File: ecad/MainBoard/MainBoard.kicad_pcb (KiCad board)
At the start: 2 copper layers, 34.6 x 88.7 mm, 10 parts, among them J1 ACJM-HHDR, J2 PJ-102A, J3 toEffectsBoard, J4 ACJM-HHDR, U1 FS57003PLT2B2M2QE

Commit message: Big commit
Spice Simulations
Finalize ECAD schematic
old MCAD stuff
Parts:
- added C10: CP, Capacitor_SMD:C_0805_2012Metric_Pad1.18x1.45mm_HandSolder, B.Cu at (88.8, 100.3)
- added C11: 20n, Capacitor_SMD:C_0805_2012Metric_Pad1.18x1.45mm_HandSolder, B.Cu at (107.9, 132.3)
- added C4: 1u, Capacitor_SMD:C_0805_2012Metric_Pad1.18x1.45mm_HandSolder, B.Cu at (113.2, 126.7)
- added C5: 51p, Capacitor_SMD:C_0805_2012Metric_Pad1.18x1.45mm_HandSolder, B.Cu at (110.2, 96.7)
- added C6: 0u22, Capacitor_SMD:C_0805_2012Metric_Pad1.18x1.45mm_HandSolder, B.Cu at (102.2, 100.6)
- added C7: 220n, Capacitor_SMD:C_0805_2012Metric_Pad1.18x1.45mm_HandSolder, B.Cu at (101.0, 76.8)
- added C8: 1u, Capacitor_SMD:C_0805_2012Metric_Pad1.18x1.45mm_HandSolder, B.Cu at (93.3, 90.3)
- added C9: 0u1, Capacitor_SMD:C_0805_2012Metric_Pad1.18x1.45mm_HandSolder, B.Cu at (86.2, 90.6)
- added D2: QBL8XX60D, digikey-footprints:LED_5mm_Radial, F.Cu at (101.3, 105.8)
- added D3: 1N914, Diode_THT:D_DO-35_SOD27_P2.54mm_Vertical_AnodeUp, F.Cu at (111.7, 80.1)
- added D4: 1N914, Diode_THT:D_DO-35_SOD27_P2.54mm_Vertical_AnodeUp, F.Cu at (114.3, 77.6)
- added G***: LOGO, screaming-panda:Panda_Logo, F.Cu at (113.7, 72.4)
- added J5: TonePot, Connector_PinHeader_2.54mm:PinHeader_1x03_P2.54mm_Vertical, F.Cu at (102.5, 79.8)
- added J6: VolumePot, Connector_PinHeader_2.54mm:PinHeader_1x03_P2.54mm_Vertical, F.Cu at (93.3, 83.3)
- added Q1: 2N4401BU, digikey-footprints:TO-92-3, F.Cu at (88.8, 92.9)
- added Q2: 2N4401BU, digikey-footprints:TO-92-3, F.Cu at (109.7, 125.0)
- added R10: 1k, Resistor_SMD:R_0805_2012Metric_Pad1.20x1.40mm_HandSolder, B.Cu at (93.3, 86.6)
- added R11: 501k, Resistor_SMD:R_0805_2012Metric_Pad1.20x1.40mm_HandSolder, B.Cu at (84.2, 90.6)
- added R12: 10k, Resistor_SMD:R_0805_2012Metric_Pad1.20x1.40mm_HandSolder, B.Cu at (85.9, 95.5)
- added R13: 100, Resistor_SMD:R_0805_2012Metric_Pad1.20x1.40mm_HandSolder, B.Cu at (88.8, 96.5)
- added R14: 10k, Resistor_SMD:R_0805_2012Metric_Pad1.20x1.40mm_HandSolder, B.Cu at (86.8, 100.3)
- added R15: 1M5, Resistor_SMD:R_0805_2012Metric_Pad1.20x1.40mm_HandSolder, B.Cu at (108.8, 135.2)
- added R16: 1k, Resistor_SMD:R_0805_2012Metric_Pad1.20x1.40mm_HandSolder, B.Cu at (107.9, 128.5)
- added R17: 501k, Resistor_SMD:R_0805_2012Metric_Pad1.20x1.40mm_HandSolder, B.Cu at (106.0, 126.5)
- added R18: 10k, Resistor_SMD:R_0805_2012Metric_Pad1.20x1.40mm_HandSolder, B.Cu at (111.2, 128.8)
- added R2: 10k, Resistor_SMD:R_0805_2012Metric_Pad1.20x1.40mm_HandSolder, B.Cu at (89.8, 70.5)
- added R3: 10k, Resistor_SMD:R_0805_2012Metric_Pad1.20x1.40mm_HandSolder, B.Cu at (91.8, 74.2)
- added R4: 10k, Resistor_SMD:R_0805_2012Metric_Pad1.20x1.40mm_HandSolder, B.Cu at (114.2, 123.8)
- added R5: 51k, Resistor_SMD:R_0805_2012Metric_Pad1.20x1.40mm_HandSolder, B.Cu at (115.0, 84.6)
- added R6: 1k, Resistor_SMD:R_0805_2012Metric_Pad1.20x1.40mm_HandSolder, B.Cu at (104.4, 97.7)
- added R7: 10k, Resistor_SMD:R_0805_2012Metric_Pad1.20x1.40mm_HandSolder, B.Cu at (104.2, 100.6)
- added R8: 220, Resistor_SMD:R_0805_2012Metric_Pad1.20x1.40mm_HandSolder, B.Cu at (101.0, 74.9)
- added R9: 1k, Resistor_SMD:R_0805_2012Metric_Pad1.20x1.40mm_HandSolder, B.Cu at (99.4, 94.2)
- added U2: RC4558, Package_SO:Texas_R-PDSO-G8_EP2.95x4.9mm_Mask2.4x3.1mm, B.Cu at (104.5, 93.9)
- C1, R1: moved to B.Cu
- C2: value 1u -> 10n; moved to B.Cu
- C3: value 10n -> 47u; moved to B.Cu
- D1: value QBL8XX60D -> 1N914; footprint Diode_THT:D_DO-201AD_P3.81mm_Vertical_AnodeUp -> Diode_THT:D_DO-35_SOD27_P2.54mm_Vertical_AnodeUp
- J3: value toEffectsBoard -> ACJM-HHDR; footprint Connector_PinHeader_1.27mm:PinHeader_2x02_P1.27mm_Vertical -> screaming-panda:ACJM-HHDR
- J4: value ACJM-HHDR -> DrivePot; footprint screaming-panda:ACJM-HHDR -> Connector_PinHeader_2.54mm:PinHeader_1x03_P2.54mm_Vertical
- moved D1 39.2 mm to (91.1, 67.3)
- moved J3 15.6 mm to (105.8, 93.8)
- moved J4 11.7 mm to (111.7, 83.6), turned to 270 degrees
- moved C1 8.35 mm to (93.7, 70.5), turned to 270 degrees
- moved C3 8.34 mm to (89.8, 74.2), turned to 270 degrees
- moved C2 6.24 mm to (91.8, 70.5), turned to 270 degrees
- moved R1 1.82 mm to (104.5, 106.8), turned to 90 degrees
- moved J1 0.22 mm to (94.2, 117.8)
- moved U1 0.10 mm to (100.0, 135.6), turned to 180 degrees
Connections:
- C3 pad 1: +9V -> VCC
- D1 pad 1: Net-(D1-Pad1) -> +9V
- D1 pad 2: Net-(D1-Pad2) -> GND
- R1 pad 2: Net-(D1-Pad2) -> Net-(D2-Pad2)
- U1 pad 1: Net-(D1-Pad1) -> Net-(D2-Pad1)
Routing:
- net /SIG_OUT: track 0.00 -> 50.7 mm
- net Net-(D1-Pad1): track 37.8 -> 0.00 mm
- net /tone/IN: track 0.00 -> 35.9 mm, vias 0 -> 1
- net /EFFECT_OUT: track 0.00 -> 35.1 mm, vias 0 -> 1
- net Net-(C4-Pad2): track 0.00 -> 34.2 mm, vias 0 -> 2
- net Net-(C5-Pad1): track 0.00 -> 33.1 mm, vias 0 -> 2
- net Net-(C5-Pad2): track 0.00 -> 28.9 mm, vias 0 -> 2
- net Net-(D2-Pad1): track 0.00 -> 27.8 mm
- net Net-(J5-Pad3): track 0.00 -> 24.1 mm, vias 0 -> 1
- net /PassThru: track 0.00 -> 20.1 mm
- net VCC: track 0.00 -> 19.9 mm, vias 0 -> 3
- net +9V: track 0.00 -> 13.8 mm, vias 0 -> 1
- net GND: track 12.0 -> 0.00 mm
- net /SIG_IN: track 0.00 -> 10.7 mm
- net /volume/IN: track 0.00 -> 10.5 mm, vias 0 -> 2
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- added copper zone on In1.Cu, net +9V
- added copper zone on F.Cu, net GND
- added copper zone on In2.Cu, net VCC
- removed copper zone on F.Cu, net +9V
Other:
- copper layers 2 -> 4

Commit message: Update BOM and SPIRCE SIM
Add netlist to calculate power dissipation through each resistor
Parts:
- added C3: 50p, Capacitor_SMD:C_0805_2012Metric_Pad1.18x1.45mm_HandSolder, F.Cu at (94.9, 30.7)
- added IC1: RC4558, Package_SO:Texas_R-PDSO-G8_EP2.95x4.9mm_Mask2.4x3.1mm, F.Cu at (81.8, 32.4)
- added R6: 4k7, Resistor_SMD:R_0805_2012Metric_Pad1.20x1.40mm_HandSolder, F.Cu at (99.7, 30.7)
- C11: renamed from C10; value CP -> 10u
- C4: renamed from C5; value 51p -> 50p
- renumbered C11 to C1, C9 to C10, C1 to C12, C4 to C2, C6 to C5, C3 to C7, C7 to C9, D3 to D1, D4 to D2, D2 to D4, D1 to D5, J3 to J2, J2 to J3, Q2 to Q1, Q1 to Q2, R16 to R1, R3 to R10, R8 to R11, R11 to R12, R14 to R13, R12 to R14, R13 to R15, R7 to R16, R9 to R17, R10 to R18, J4 to R19, R17 to R2, J5 to R20, J6 to R21, R15 to R22, R1 to R23, R18 to R3, R4 to R5, R5 to R7, R6 to R8, R2 to R9, U1 to SW1
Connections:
- C10 pad 2: Net-(C9-Pad2) (its old number) -> Net-(C10-Pad2)
- C12 pad 2: GND -> 0
- C2 pad 2: Net-(C4-Pad2) -> Net-(C2-Pad2)
- C4 pad 1: Net-(C5-Pad1) -> Net-(C3-Pad1)
- C4 pad 2: Net-(C5-Pad2) -> Net-(C4-Pad2)
- C5 pad 2: GND -> 0
- C7 pad 2: GND -> 0
- D1 pad 1: Net-(C5-Pad1) -> Net-(C3-Pad1)
- D1 pad 2: Net-(C5-Pad2) -> Net-(C4-Pad2)
- D2 pad 1: Net-(C5-Pad2) -> Net-(C4-Pad2)
- D2 pad 2: Net-(C5-Pad1) -> Net-(C3-Pad1)
- D4 pad 1: Net-(D2-Pad1) -> Net-(D4-Pad1)
- D5 pad 2: GND -> 0
- J1 pad S: GND -> 0
- J1 pad SN: GND -> 0
- J1 pad TN: GND -> 0
- J2 pad S: GND -> 0
- J2 pad SN: (no net) -> Net-(J2-PadSN)
- J2 pad TN: (no net) -> Net-(J2-PadTN)
- J3 pad 1: GND -> 0
- J3 pad 3: GND -> 0
- R10 pad 2: GND -> 0
- R11 pad 2: GND -> 0
- R12 pad 2: GND -> VCC
- R13 pad 2: GND -> 0
- R14 pad 2: GND -> 0
- R17 pad 2: Net-(J5-Pad3) -> Net-(IC1-Pad6)
- R19 pad 1: Net-(J4-Pad1) -> Net-(R19-Pad1)
- R19 pad 2: (no net) -> Net-(C4-Pad2)
- R19 pad 3: Net-(C5-Pad1) -> Net-(R19-Pad3)
- R20 pad 3: Net-(J5-Pad3) -> Net-(IC1-Pad6)
- R21 pad 2: VCC -> Net-(C10-Pad2)
- R21 pad 3: Net-(C9-Pad2) (its old number) -> VCC
- R22 pad 2: GND -> 0
- R3 pad 2: GND -> 0
- R5 pad 2: Net-(C4-Pad2) -> Net-(C2-Pad2)
- R7 pad 1: Net-(J4-Pad1) -> Net-(R19-Pad3)
- R7 pad 2: Net-(C5-Pad2) -> Net-(C3-Pad1)
- R8 pad 2: Net-(C5-Pad1) -> Net-(C4-Pad2)
- SW1 pad 1: Net-(D2-Pad1) -> /PassThru
- SW1 pad 2: GND -> /SIG_IN
- SW1 pad 4: /PassThru -> Net-(D4-Pad1)
- SW1 pad 5: /SIG_IN -> 0
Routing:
- net Net-(C9-Pad2): track 1.99 -> 9.06 mm
- net Net-(C9-Pad2) (its old number): track 7.07 -> 0.00 mm
- added copper zone on F.Cu, net /SIG_IN
- added copper zone on B.Cu, net VCC
- removed copper zone on B.Cu, net GND
- removed copper zone on F.Cu, net GND

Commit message: Clean up ecad
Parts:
- removed the C2 at (113.2, 126.7)
- removed the C2 at (91.8, 70.5)
- removed Q1, Q2: 2N4401BU, digikey-footprints:TO-92-3
- removed U2: RC4558, Package_SO:Texas_R-PDSO-G8_EP2.95x4.9mm_Mask2.4x3.1mm
- added C2: 1u, Capacitor_SMD:C_0603_1608Metric_Pad1.08x0.95mm_HandSolder, F.Cu at (52.7, 66.2)
- C1, C5: footprint Capacitor_SMD:C_0805_2012Metric_Pad1.18x1.45mm_HandSolder -> Capacitor_SMD:C_0402_1005Metric_Pad0.74x0.62mm_HandSolder; moved to F.Cu
- C10, C4: footprint Capacitor_SMD:C_0805_2012Metric_Pad1.18x1.45mm_HandSolder -> Capacitor_SMD:C_0201_0603Metric_Pad0.64x0.40mm_HandSolder; moved to F.Cu
- C11, C8: footprint Capacitor_SMD:C_0805_2012Metric_Pad1.18x1.45mm_HandSolder -> Capacitor_SMD:C_0603_1608Metric_Pad1.08x0.95mm_HandSolder; moved to F.Cu
- C12: footprint Capacitor_SMD:C_0805_2012Metric_Pad1.18x1.45mm_HandSolder -> Capacitor_SMD:C_1210_3225Metric_Pad1.33x2.70mm_HandSolder; moved to F.Cu
- C3: footprint Capacitor_SMD:C_0805_2012Metric_Pad1.18x1.45mm_HandSolder -> Capacitor_SMD:C_0201_0603Metric_Pad0.64x0.40mm_HandSolder
- C7, C9: footprint Capacitor_SMD:C_0805_2012Metric_Pad1.18x1.45mm_HandSolder -> Capacitor_SMD:C_1206_3216Metric_Pad1.33x1.80mm_HandSolder; moved to F.Cu
- G***: moved to B.Cu
- IC1: footprint Package_SO:Texas_R-PDSO-G8_EP2.95x4.9mm_Mask2.4x3.1mm -> DigiKey:SOIC-8_W3.9mm
- R1, R17, R18, R22, R23, R8: footprint Resistor_SMD:R_0805_2012Metric_Pad1.20x1.40mm_HandSolder -> Resistor_SMD:R_0402_1005Metric_Pad0.72x0.64mm_HandSolder; moved to F.Cu
- R10, R13, R14, R16, R3, R5, R9: moved to F.Cu
- R11: footprint Resistor_SMD:R_0805_2012Metric_Pad1.20x1.40mm_HandSolder -> Resistor_SMD:R_2512_6332Metric_Pad1.40x3.35mm_HandSolder; moved to F.Cu
- R12: value 501k -> 510k; moved to F.Cu
- R15: footprint Resistor_SMD:R_0805_2012Metric_Pad1.20x1.40mm_HandSolder -> Resistor_SMD:R_1218_3246Metric_Pad1.22x4.75mm_HandSolder; moved to F.Cu
- R19: value DrivePot -> 500ka
- R2: value 501k -> 505k; moved to F.Cu
- R20: value TonePot -> 20kb
- R21: value VolumePot -> 20ka
- R7: footprint Resistor_SMD:R_0805_2012Metric_Pad1.20x1.40mm_HandSolder -> Resistor_SMD:R_1206_3216Metric_Pad1.30x1.75mm_HandSolder; moved to F.Cu
- moved R5 87.5 mm to (48.2, 66.4), turned to 0 degrees
- moved R23 84.9 mm to (40.9, 50.4), turned to 0 degrees
- moved R22 83.1 mm to (64.5, 64.8)
- moved R3 78.2 mm to (70.0, 62.3), turned to 0 degrees
- moved C1 77.0 mm to (71.0, 64.8), turned to 0 degrees
- moved R2 76.0 mm to (65.3, 62.3), turned to 0 degrees
- moved R1 75.3 mm to (67.8, 64.8), turned to 0 degrees
- moved R7 69.5 mm to (48.8, 63.3), turned to 0 degrees
- moved R18 66.8 mm to (28.9, 68.9), turned to 0 degrees
- moved R15 66.6 mm to (30.2, 64.8), turned to 0 degrees
- moved R16 62.6 mm to (54.1, 63.1), turned to 0 degrees
- moved C4 62.3 mm to (56.3, 65.5), turned to 0 degrees
- moved C11 62.1 mm to (35.3, 68.8), turned to 0 degrees
- moved R13 61.7 mm to (35.5, 66.0), turned to 0 degrees
- moved R17 60.8 mm to (57.3, 50.4), turned to 0 degrees
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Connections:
- C8 pad 1: Net-(C8-Pad1) -> /volume/IN
- C8 pad 2: /volume/IN -> Net-(C8-Pad2)
- J2 pad SN: Net-(J2-PadSN) -> 0
- J2 pad TN: Net-(J2-PadTN) -> 0
- R11 pad 1: Net-(C9-Pad2) -> Net-(C9-Pad1)
- R12 pad 1: Net-(C10-Pad1) -> VCC
- R12 pad 2: VCC -> Net-(C10-Pad1)
- R18 pad 2: Net-(C8-Pad1) -> Net-(C8-Pad2)
- R20 pad 2: Net-(C9-Pad1) -> Net-(C9-Pad2)
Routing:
- net /SIG_OUT: track 50.7 -> 0.00 mm
- net /tone/IN: track 35.9 -> 0.00 mm, vias 1 -> 0
- net /EFFECT_OUT: track 35.1 -> 0.00 mm, vias 1 -> 0
- net Net-(C4-Pad2): track 34.2 -> 0.00 mm, vias 2 -> 0
- net Net-(C5-Pad1): track 33.1 -> 0.00 mm, vias 2 -> 0
- net Net-(C5-Pad2): track 28.9 -> 0.00 mm, vias 2 -> 0
- net Net-(D2-Pad1): track 27.8 -> 0.00 mm
- net Net-(J5-Pad3): track 24.1 -> 0.00 mm, vias 1 -> 0
- net 0: track 0.00 -> 21.2 mm
- net /PassThru: track 20.1 -> 0.00 mm
- net VCC: track 19.9 -> 0.00 mm, vias 3 -> 0
- net /SIG_IN: track 10.7 -> 0.00 mm
- net /volume/IN: track 10.5 -> 0.00 mm, vias 2 -> 0
- net Net-(C9-Pad2): track 9.06 -> 0.00 mm
- net Net-(Q1-Pad2): track 7.05 -> 0.00 mm
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- added copper zone on B.Cu, net 0
- added copper zone on F.Cu, net VCC
- removed copper zone on In1.Cu, net +9V
- removed copper zone on F.Cu, net /SIG_IN
- removed copper zone on B.Cu, net VCC
- removed copper zone on In2.Cu, net VCC
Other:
- copper layers 4 -> 2

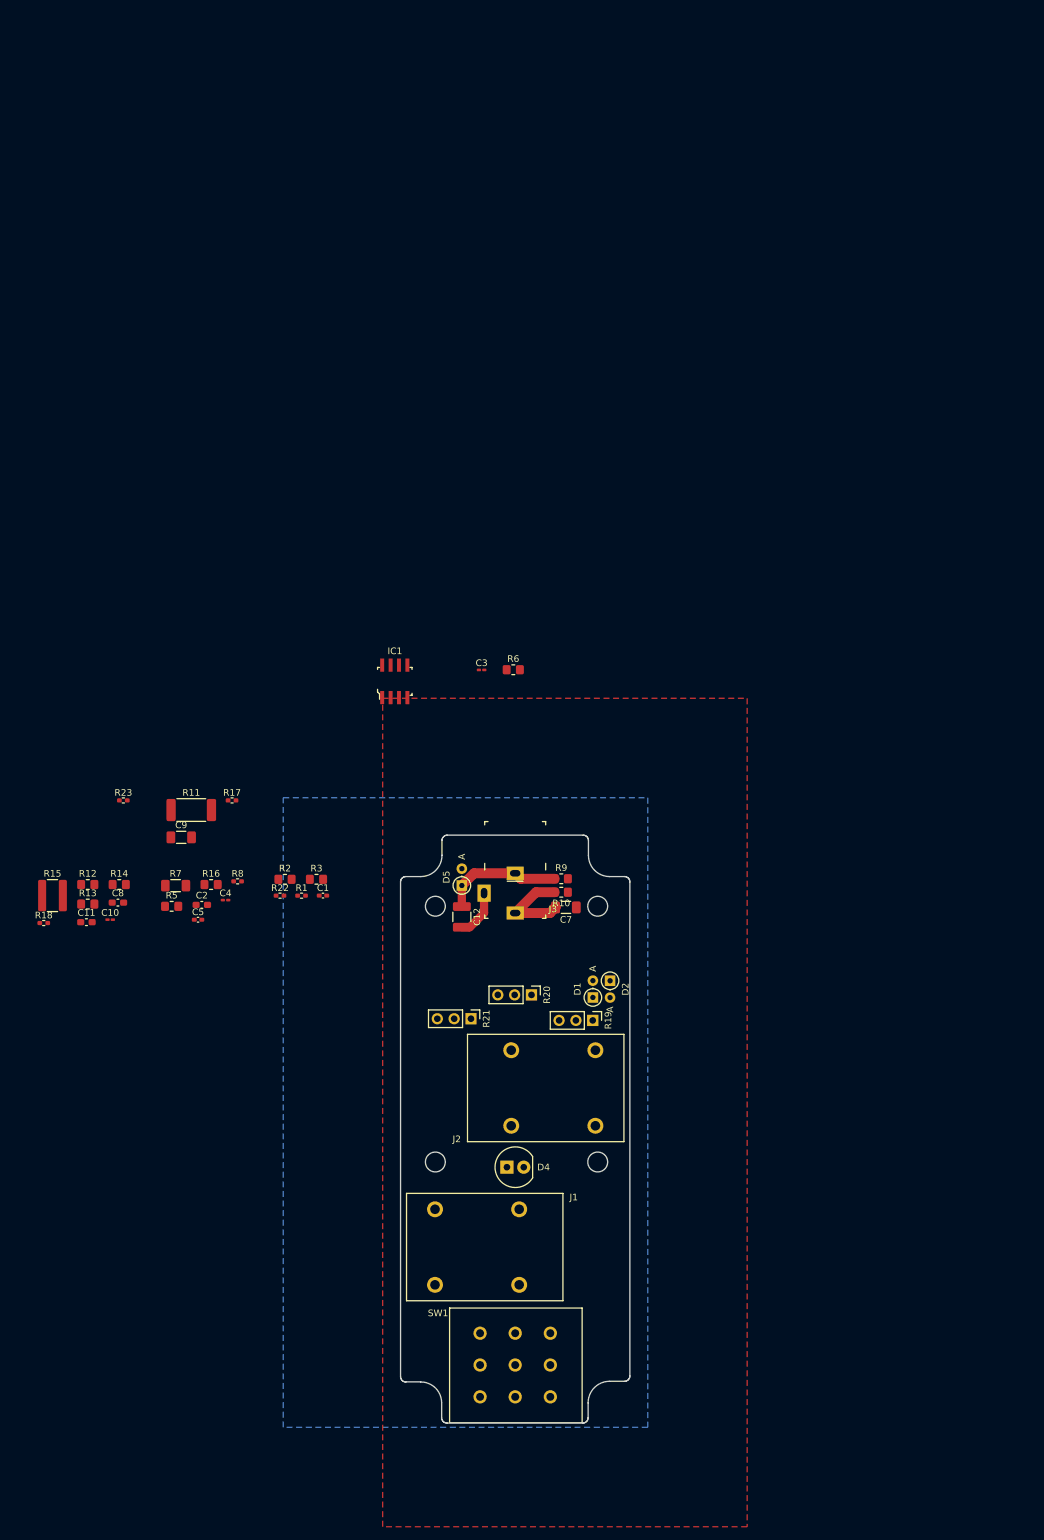
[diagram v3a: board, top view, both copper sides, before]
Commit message: Update layouts with finished mcad
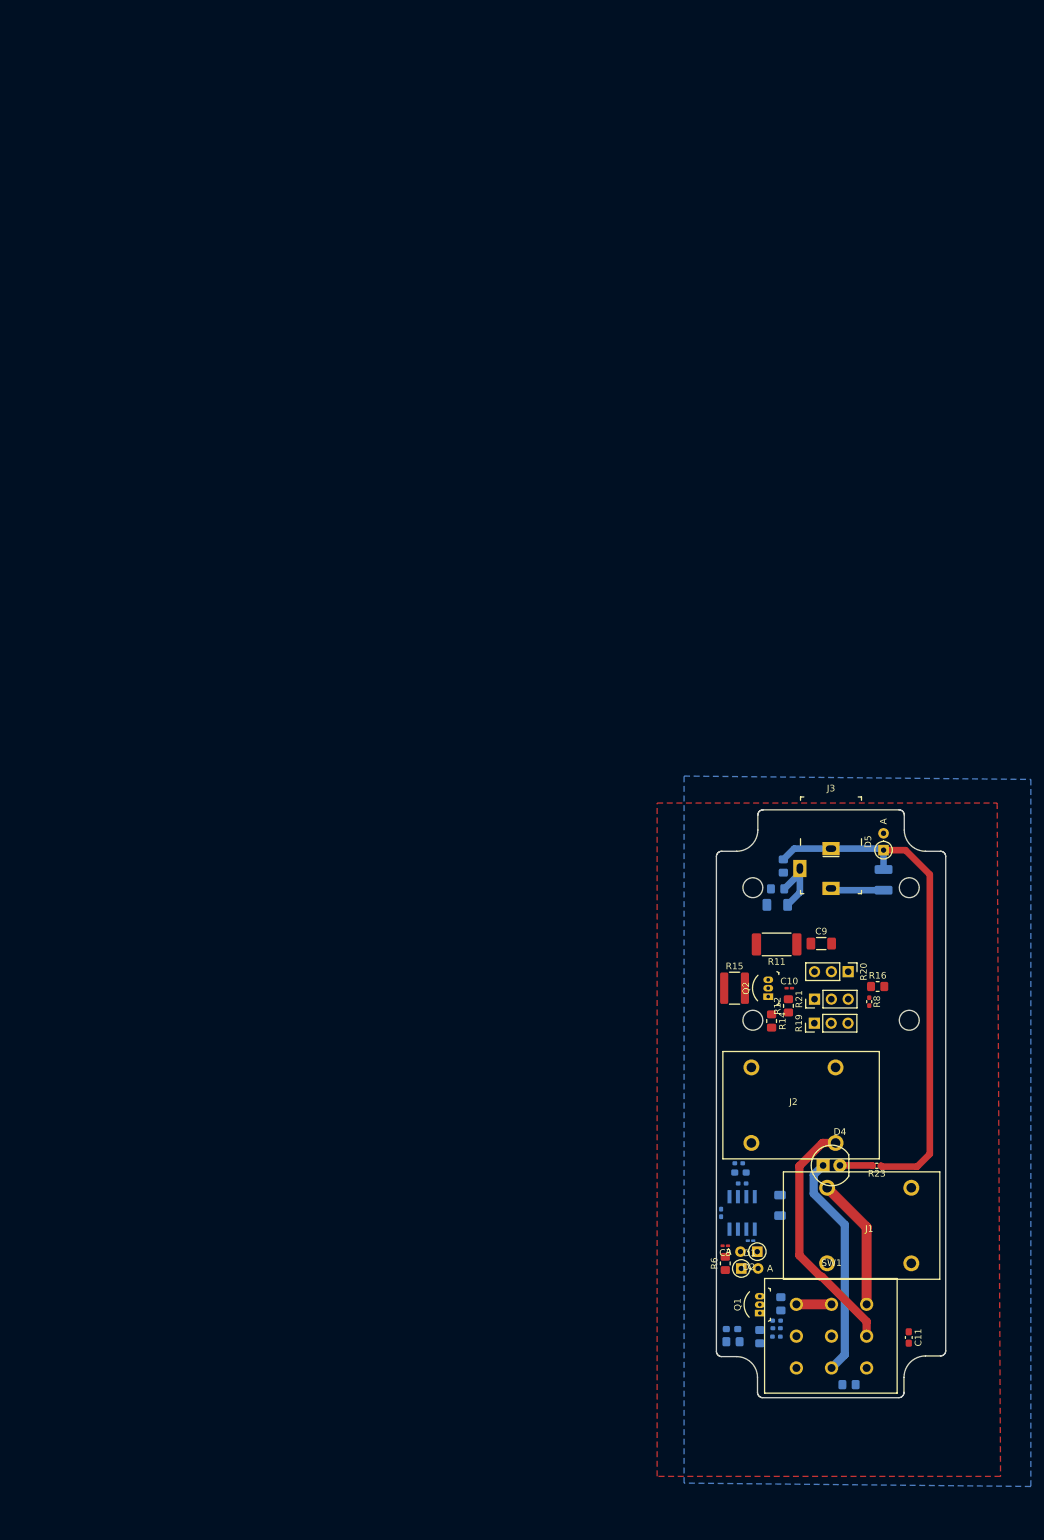
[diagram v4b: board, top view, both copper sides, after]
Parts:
- removed G***: LOGO, screaming-panda:Panda_Logo
- added Q1: 2N4401BU, DigiKey:TO-92-3, F.Cu at (136.9, 127.8)
- added Q2: 2N4401BU, DigiKey:TO-92-3, F.Cu at (138.2, 80.0)
- C1, C12, C2, C4, C5, C7, C8, IC1, R1, R10, R13, R17, R18, R2, R22, R3, R5, R7, R9: moved to B.Cu
- D4: footprint digikey-footprints:LED_5mm_Radial -> DigiKey:LED_5mm_Radial
- moved C11 139.0 mm to (159.4, 131.4), turned to 270 degrees
- moved R13 135.8 mm to (150.4, 138.6), turned to 180 degrees
- moved R23 126.3 mm to (154.6, 105.5), turned to 180 degrees
- moved R18 111.0 mm to (133.7, 105.2), turned to 180 degrees
- moved R12 107.3 mm to (141.2, 81.4), turned to 90 degrees
- moved R5 107.2 mm to (132.9, 132.1), turned to 180 degrees
- moved R15 103.9 mm to (133.1, 78.7)
- moved R7 103.2 mm to (140.0, 111.5), turned to 270 degrees
- moved C10 103.0 mm to (141.4, 78.7)
- moved C2 102.5 mm to (132.7, 130.2), turned to 180 degrees
- moved C8 102.4 mm to (134.0, 106.6), turned to 180 degrees
- moved R16 101.7 mm to (154.7, 78.5)
- moved R14 100.6 mm to (138.7, 83.7), turned to 270 degrees
- moved R22 100.2 mm to (139.4, 131.3), turned to 180 degrees
- moved R2 98.5 mm to (140.1, 126.4), turned to 270 degrees
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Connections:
- R19 pad 1: Net-(R19-Pad1) -> (no net)
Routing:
- net +9V: track 18.3 -> 77.7 mm
- net /SIG_OUT: track 0.00 -> 36.9 mm
- net Net-(D4-Pad1): track 0.00 -> 33.9 mm
- net /PassThru: track 0.00 -> 20.1 mm
- net Net-(SW1-Pad3): track 0.00 -> 5.30 mm
- net Net-(D4-Pad2): track 0.00 -> 4.98 mm
- net 0: track 21.2 -> 18.3 mm
- added copper zone on F.Cu, net 0
- added copper zone on B.Cu, net VCC
- removed copper zone on B.Cu, net 0
- removed copper zone on F.Cu, net VCC
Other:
- outline, holes or cut-outs redrawn
